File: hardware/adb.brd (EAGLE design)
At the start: 24.1 x 12.7 mm, 10 parts, among them U1 Tiny85-20-SMT

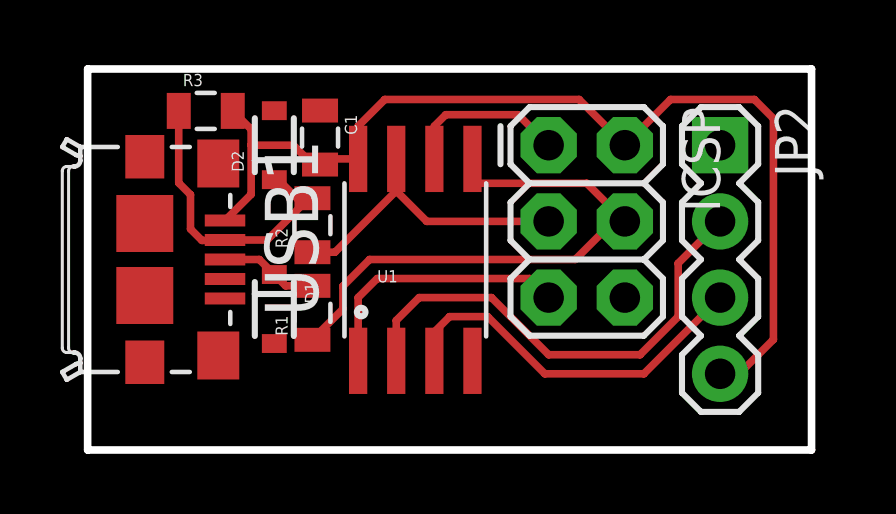
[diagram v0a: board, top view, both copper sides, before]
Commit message: hardware: bumped ICSP up, rearranged Rs and Ds.
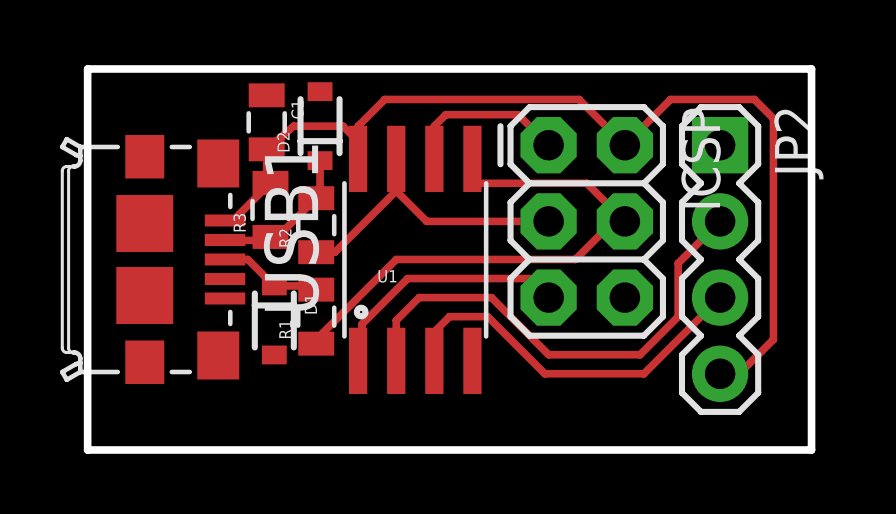
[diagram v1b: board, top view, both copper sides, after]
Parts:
- moved R3 3.95 mm to (6.10, 8.00), turned to 90 degrees
- moved C1 1.85 mm to (5.97, 10.9)
- moved D2 1.65 mm to (7.75, 10.8)
- moved D1 0.38 mm to (6.22, 4.32)
- moved R1 0.18 mm to (7.62, 4.45)
- moved R2 0.13 mm to (7.62, 7.49)
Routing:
- net D-: track 10.5 -> 4.93 mm
- net VCC: track 34.8 -> 33.4 mm
- net RESET: track 8.98 -> 8.39 mm
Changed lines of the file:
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@@
 </autorouter>
 <elements>
-<element name="C1" library="SparkFun-Capacitors" package="0805" value="1uF" x="7.747" y="10.414" rot="R270">
-<attribute name="PROD_ID" value="CAP-11625" x="7.747" y="10.414" size="1.778" layer="27" rot="R270" display="off"/>
+<element name="C1" library="SparkFun-Capacitors" package="0805" value="1uF" x="5.969" y="10.922" rot="R270">
+<attribute name="PROD_ID" value="CAP-11625" x="5.969" y="10.922" size="1.778" layer="27" rot="R270" display="off"/>
 </element>
-<element name="D1" library="SparkFun-DiscreteSemi" package="SOD-323" value="3.6V" x="6.223" y="4.699" rot="R270">
-<attribute name="PROD_ID" value="DIO-11284" x="6.223" y="4.699" size="1.778" layer="27" rot="R270" display="off"/>
+<element name="D1" library="SparkFun-DiscreteSemi" package="SOD-323" value="3.6V" x="6.223" y="4.318" rot="R270">
+<attribute name="PROD_ID" value="DIO-11284" x="6.223" y="4.318" size="1.778" layer="27" rot="R270" display="off"/>
 </element>
-<element name="D2" library="SparkFun-DiscreteSemi" package="SOD-323" value="3.6V" x="6.223" y="10.16" rot="R90">
-<attribute name="PROD_ID" value="DIO-11284" x="6.223" y="10.16" size="1.778" layer="27" rot="R90" display="off"/>
+<element name="D2" library="SparkFun-DiscreteSemi" package="SOD-323" value="3.6V" x="7.747" y="10.795" rot="R90">
+<attribute name="PROD_ID" value="DIO-11284" x="7.747" y="10.795" size="1.778" layer="27" rot="R90" display="off"/>
 </element>
 <element name="JP2" library="SparkFun-Connectors" package="1X04" value="" x="21.082" y="10.16" rot="R270"/>
-<element name="R1" library="SparkFun-Passives" package="0805" value="68R" x="7.493" y="4.572" rot="R90"/>
-<element name="R2" library="SparkFun-Passives" package="0805" value="68R" x="7.493" y="7.493" rot="R90"/>
+<element name="R1" library="SparkFun-Passives" package="0805" value="68R" x="7.62" y="4.445" rot="R90"/>
+<element name="R2" library="SparkFun-Passives" package="0805" value="68R" x="7.62" y="7.493" rot="R90"/>
 <element name="U1" library="SparkFun-DigitalIC" package="SO08-EIAJ" value="Tiny85-20-SMT" x="10.922" y="6.35">
 <attribute name="PROD_ID" value="IC-09092" x="10.922" y="6.35" size="1.778" layer="27" display="off"/>
@@
 <element name="ICSP" library="SparkFun-Connectors" package="2X3" value="" x="15.367" y="10.16" rot="R270"/>
 <element name="USB1" library="dangerousprototypes_devices" package="CONN_USB_MICRO-B" value="" x="1.905" y="6.35" rot="R270"/>
-<element name="R3" library="SparkFun-Passives" package="0805" value="2K2" x="3.937" y="11.303"/>
+<element name="R3" library="SparkFun-Passives" package="0805" value="2K2" x="6.096" y="8.001" rot="R90"/>
 </elements>
 <signals>
@@
 <contactref element="JP2" pad="4"/>
 <contactref element="USB1" pad="P1"/>
-<wire x1="4.58" y1="7.65" x2="5.45" y2="8.52" width="0.254" layer="1"/>
-<wire x1="5.45" y1="10.69" x2="5.45" y2="10.16" width="0.254" layer="1"/>
-<wire x1="5.45" y1="10.16" x2="5.45" y2="8.52" width="0.254" layer="1"/>
 <wire x1="17.907" y1="10.16" x2="16.383" y2="11.684" width="0.254" layer="1"/>
 <wire x1="22.86" y1="11.049" x2="22.86" y2="3.683" width="0.254" layer="1"/>
@@
 <wire x1="16.383" y1="11.684" x2="9.906" y2="11.684" width="0.254" layer="1"/>
 <wire x1="9.906" y1="11.684" x2="9.017" y2="10.795" width="0.254" layer="1"/>
-<wire x1="9.017" y1="10.795" x2="9.017" y2="9.7028" width="0.254" layer="1"/>
-<wire x1="7.747" y1="9.514" x2="7.504" y2="9.514" width="0.254" layer="1"/>
-<wire x1="7.504" y1="9.514" x2="6.858" y2="10.16" width="0.254" layer="1"/>
-<wire x1="6.858" y1="10.16" x2="5.45" y2="10.16" width="0.254" layer="1"/>
-<wire x1="7.747" y1="9.514" x2="7.9358" y2="9.7028" width="0.254" layer="1"/>
-<wire x1="7.9358" y1="9.7028" x2="9.017" y2="9.7028" width="0.254" layer="1"/>
+<wire x1="9.017" y1="10.795" x2="9.017" y2="10.287" width="0.254" layer="1"/>
 <contactref element="R3" pad="2"/>
+<wire x1="9.017" y1="10.287" x2="9.017" y2="9.7028" width="0.254" layer="1"/>
 <wire x1="17.907" y1="10.16" x2="19.431" y2="11.684" width="0.254" layer="1"/>
 <wire x1="19.431" y1="11.684" x2="22.225" y2="11.684" width="0.254" layer="1"/>
 <wire x1="22.225" y1="11.684" x2="22.86" y2="11.049" width="0.254" layer="1"/>
-<wire x1="5.45" y1="10.69" x2="4.837" y2="11.303" width="0.254" layer="1"/>
+<wire x1="5.969" y1="10.022" x2="6.869" y2="10.795" width="0.254" layer="1"/>
+<wire x1="6.869" y1="10.795" x2="8.509" y2="10.795" width="0.254" layer="1"/>
+<wire x1="8.509" y1="10.795" x2="9.017" y2="10.287" width="0.254" layer="1"/>
+<wire x1="4.58" y1="7.65" x2="4.845" y2="7.65" width="0.254" layer="1"/>
+<wire x1="4.845" y1="7.65" x2="6.096" y2="8.901" width="0.254" layer="1"/>
+<wire x1="5.969" y1="10.022" x2="5.969" y2="9.028" width="0.254" layer="1"/>
+<wire x1="5.969" y1="9.028" x2="6.096" y2="8.901" width="0.254" layer="1"/>
 </signal>
 <signal name="GND">
@@
 <wire x1="10.287" y1="9.7028" x2="10.287" y2="8.636" width="0.254" layer="1"/>
 <wire x1="10.287" y1="8.636" x2="8.244" y2="6.593" width="0.254" layer="1"/>
-<wire x1="7.493" y1="6.593" x2="8.244" y2="6.593" width="0.254" layer="1"/>
 <wire x1="10.287" y1="8.636" x2="11.303" y2="7.62" width="0.254" layer="1"/>
 <wire x1="11.303" y1="7.62" x2="15.367" y2="7.62" width="0.254" layer="1"/>
+<wire x1="7.62" y1="6.593" x2="8.244" y2="6.593" width="0.254" layer="1"/>
 </signal>
 <signal name="D-">
@@
 <contactref element="USB1" pad="P2"/>
 <wire x1="4.58" y1="7" x2="4.595" y2="6.985" width="0.254" layer="1"/>
-<wire x1="6.223" y1="9.01" x2="6.357" y2="9.01" width="0.254" layer="1"/>
-<wire x1="6.357" y1="9.01" x2="6.985" y2="8.382" width="0.254" layer="1"/>
-<wire x1="6.985" y1="8.382" x2="7.482" y2="8.382" width="0.254" layer="1"/>
-<wire x1="7.482" y1="8.382" x2="7.493" y2="8.393" width="0.254" layer="1"/>
-<wire x1="4.58" y1="7" x2="5.984" y2="7" width="0.254" layer="1"/>
-<wire x1="5.984" y1="7" x2="7.377" y2="8.393" width="0.254" layer="1"/>
-<wire x1="7.377" y1="8.393" x2="7.493" y2="8.393" width="0.254" layer="1"/>
 <contactref element="R3" pad="1"/>
-<wire x1="3.037" y1="11.303" x2="3.037" y2="8.901" width="0.254" layer="1"/>
-<wire x1="3.037" y1="8.901" x2="3.429" y2="8.509" width="0.254" layer="1"/>
-<wire x1="3.429" y1="8.509" x2="3.429" y2="7.366" width="0.254" layer="1"/>
-<wire x1="3.429" y1="7.366" x2="3.81" y2="6.985" width="0.254" layer="1"/>
-<wire x1="3.81" y1="6.985" x2="4.565" y2="6.985" width="0.254" layer="1"/>
-<wire x1="4.565" y1="6.985" x2="4.58" y2="7" width="0.254" layer="1"/>
+<wire x1="4.595" y1="6.985" x2="5.98" y2="6.985" width="0.254" layer="1"/>
+<wire x1="5.98" y1="6.985" x2="6.096" y2="7.101" width="0.254" layer="1"/>
+<wire x1="6.096" y1="7.101" x2="6.328" y2="7.101" width="0.254" layer="1"/>
+<wire x1="6.328" y1="7.101" x2="7.62" y2="8.393" width="0.254" layer="1"/>
+<wire x1="7.747" y1="9.645" x2="7.747" y2="8.52" width="0.254" layer="1"/>
+<wire x1="7.747" y1="8.52" x2="7.62" y2="8.393" width="0.254" layer="1"/>
 </signal>
 <signal name="D+">
@@
 <contactref element="D1" pad="C"/>
 <contactref element="USB1" pad="P3"/>
-<wire x1="4.58" y1="6.35" x2="5.722" y2="6.35" width="0.254" layer="1"/>
-<wire x1="5.722" y1="6.35" x2="6.223" y2="5.849" width="0.254" layer="1"/>
-<wire x1="6.223" y1="5.849" x2="6.6" y2="5.472" width="0.254" layer="1"/>
-<wire x1="6.6" y1="5.472" x2="7.493" y2="5.472" width="0.254" layer="1"/>
+<wire x1="4.58" y1="6.35" x2="5.341" y2="6.35" width="0.254" layer="1"/>
+<wire x1="5.341" y1="6.35" x2="6.223" y2="5.468" width="0.254" layer="1"/>
+<wire x1="6.223" y1="5.468" x2="7.497" y2="5.468" width="0.254" layer="1"/>
+<wire x1="7.497" y1="5.468" x2="7.62" y2="5.345" width="0.254" layer="1"/>
 </signal>
 <signal name="MOSI">
@@
 <wire x1="17.907" y1="7.62" x2="17.526" y2="7.62" width="0.254" layer="1"/>
 <wire x1="17.526" y1="7.62" x2="16.256" y2="6.35" width="0.254" layer="1"/>
-<wire x1="7.493" y1="3.672" x2="7.493" y2="3.683" width="0.254" layer="1"/>
-<wire x1="7.493" y1="3.683" x2="8.509" y2="4.699" width="0.254" layer="1"/>
-<wire x1="8.509" y1="4.699" x2="8.509" y2="5.461" width="0.254" layer="1"/>
-<wire x1="8.509" y1="5.461" x2="9.398" y2="6.35" width="0.254" layer="1"/>
-<wire x1="9.398" y1="6.35" x2="16.256" y2="6.35" width="0.254" layer="1"/>
+<wire x1="10.287" y1="6.35" x2="16.256" y2="6.35" width="0.254" layer="1"/>
+<wire x1="10.287" y1="6.35" x2="7.62" y2="3.683" width="0.254" layer="1"/>
+<wire x1="7.62" y1="3.683" x2="7.62" y2="3.545" width="0.254" layer="1"/>
 </signal>
 <signal name="MISO">
@@
 <contactref element="U1" pad="1"/>
 <contactref element="ICSP" pad="5"/>
-<wire x1="9.017" y1="2.9718" x2="9.017" y2="5.08" width="0.254" layer="1"/>
-<wire x1="9.017" y1="5.08" x2="9.652" y2="5.715" width="0.254" layer="1"/>
-<wire x1="9.652" y1="5.715" x2="14.732" y2="5.715" width="0.254" layer="1"/>
+<wire x1="10.668" y1="5.715" x2="14.732" y2="5.715" width="0.254" layer="1"/>
 <wire x1="14.732" y1="5.715" x2="15.367" y2="5.08" width="0.254" layer="1"/>
+<wire x1="10.668" y1="5.715" x2="9.144" y2="4.191" width="0.254" layer="1"/>
+<wire x1="9.144" y1="4.191" x2="9.144" y2="3.937" width="0.254" layer="1"/>
+<wire x1="9.144" y1="3.937" x2="9.017" y2="3.81" width="0.254" layer="1"/>
+<wire x1="9.017" y1="3.81" x2="9.017" y2="2.9718" width="0.254" layer="1"/>
 </signal>
 <signal name="N$2">

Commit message: hardware: AVR reset pulled high.
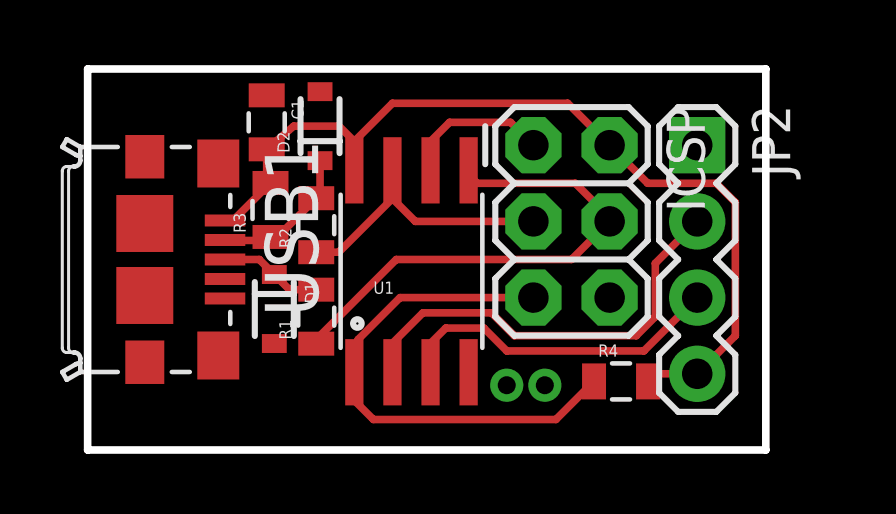
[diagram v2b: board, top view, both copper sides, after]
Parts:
- added R4: 10K, SparkFun-Passives:0805
- moved JP2 0.76 mm to (20.3, 10.2)
- moved ICSP 0.51 mm to (14.9, 10.2)
- moved U1 0.40 mm to (10.8, 5.97)
- moved D1 0.38 mm to (6.22, 4.70)
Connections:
- net RESET: now also R4.1
- net VCC: now also R4.2
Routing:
- net RESET: track 8.39 -> 17.3 mm
- net VCC: track 33.4 -> 30.4 mm
- net N$5: track 16.1 -> 14.5 mm
- net MOSI: track 18.6 -> 17.1 mm
- net N$2: track 12.5 -> 11.1 mm
- net SCK: track 10.1 -> 9.24 mm
- net MISO: track 5.48 -> 4.97 mm
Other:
- board size 24.1 x 12.7 mm -> 22.6 x 12.7 mm

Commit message: hardware: tweaks; Eagle 7.2 upgrade.
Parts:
- moved D2 0.38 mm to (7.75, 10.4)
- moved R2 0.18 mm to (7.75, 7.37)
- moved R3 0.18 mm to (6.22, 7.87)
- moved C1 0.13 mm to (5.97, 10.8)

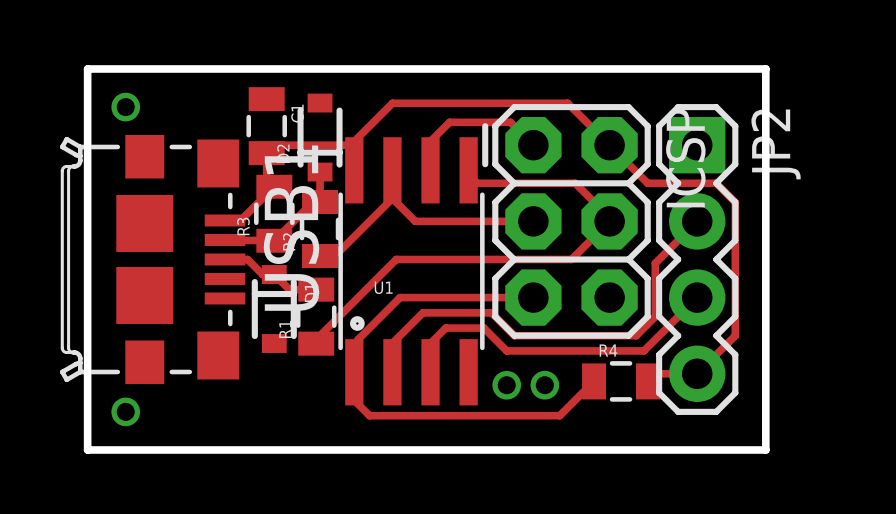
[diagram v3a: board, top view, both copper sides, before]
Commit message: hardware: polish; silk screen text etc.
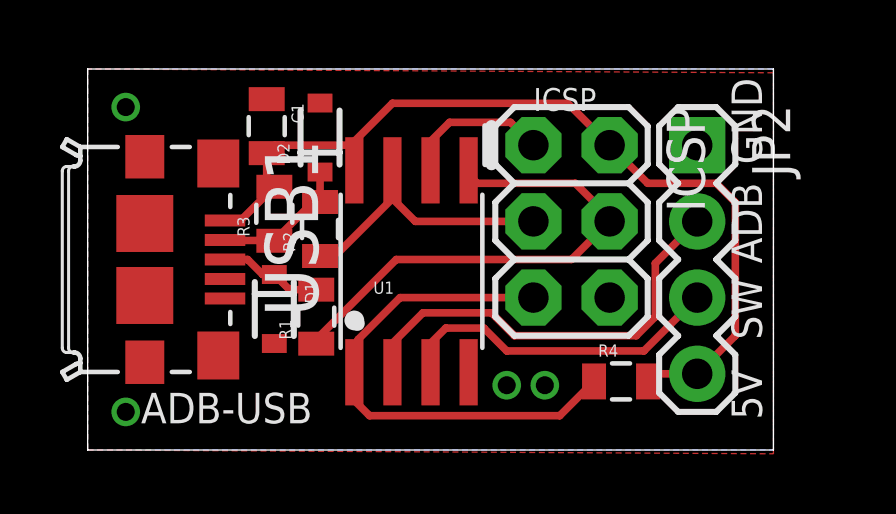
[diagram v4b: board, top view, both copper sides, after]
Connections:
- net N$2 renamed PB4
- net N$5 renamed PB3
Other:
- board size 22.6 x 12.7 mm -> 22.9 x 12.7 mm
- board text added: "5V"
- board text added: "ADB"
- board text added: "ADB-USB"
- board text added: "Apple Extended Keyboard II USB adapter @pda 2015"
- board text added: "GND"
- board text added: "ICSP"
- board text added: "SW"
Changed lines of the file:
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@@
 <layer number="20" name="Dimension" color="15" fill="1" visible="yes" active="yes"/>
 <layer number="21" name="tPlace" color="7" fill="1" visible="no" active="yes"/>
-<layer number="22" name="bPlace" color="7" fill="1" visible="yes" active="yes"/>
+<layer number="22" name="bPlace" color="7" fill="1" visible="no" active="yes"/>
 <layer number="23" name="tOrigins" color="15" fill="1" visible="yes" active="yes"/>
 <layer number="24" name="bOrigins" color="15" fill="1" visible="yes" active="yes"/>
@@
 <layer number="29" name="tStop" color="7" fill="3" visible="yes" active="yes"/>
 <layer number="30" name="bStop" color="7" fill="6" visible="yes" active="yes"/>
-<layer number="31" name="tCream" color="7" fill="4" visible="no" active="yes"/>
-<layer number="32" name="bCream" color="7" fill="5" visible="no" active="yes"/>
-<layer number="33" name="tFinish" color="6" fill="3" visible="no" active="yes"/>
-<layer number="34" name="bFinish" color="6" fill="6" visible="no" active="yes"/>
-<layer number="35" name="tGlue" color="7" fill="4" visible="no" active="yes"/>
-<layer number="36" name="bGlue" color="7" fill="5" visible="no" active="yes"/>
-<layer number="37" name="tTest" color="7" fill="1" visible="no" active="yes"/>
-<layer number="38" name="bTest" color="7" fill="1" visible="no" active="yes"/>
+<layer number="31" name="tCream" color="7" fill="4" visible="yes" active="yes"/>
+<layer number="32" name="bCream" color="7" fill="5" visible="yes" active="yes"/>
+<layer number="33" name="tFinish" color="6" fill="3" visible="yes" active="yes"/>
+<layer number="34" name="bFinish" color="6" fill="6" visible="yes" active="yes"/>
+<layer number="35" name="tGlue" color="7" fill="4" visible="yes" active="yes"/>
+<layer number="36" name="bGlue" color="7" fill="5" visible="yes" active="yes"/>
+<layer number="37" name="tTest" color="7" fill="1" visible="yes" active="yes"/>
+<layer number="38" name="bTest" color="7" fill="1" visible="yes" active="yes"/>
 <layer number="39" name="tKeepout" color="4" fill="11" visible="yes" active="yes"/>
 <layer number="40" name="bKeepout" color="1" fill="11" visible="yes" active="yes"/>
@@
 <layer number="42" name="bRestrict" color="1" fill="10" visible="yes" active="yes"/>
 <layer number="43" name="vRestrict" color="2" fill="10" visible="yes" active="yes"/>
-<layer number="44" name="Drills" color="7" fill="1" visible="yes" active="yes"/>
+<layer number="44" name="Drills" color="7" fill="1" visible="no" active="yes"/>
 <layer number="45" name="Holes" color="7" fill="1" visible="yes" active="yes"/>
 <layer number="46" name="Milling" color="3" fill="1" visible="yes" active="yes"/>
-<layer number="47" name="Measures" color="7" fill="1" visible="no" active="yes"/>
-<layer number="48" name="Document" color="7" fill="1" visible="no" active="yes"/>
-<layer number="49" name="Reference" color="7" fill="1" visible="no" active="yes"/>
+<layer number="47" name="Measures" color="7" fill="1" visible="yes" active="yes"/>
+<layer number="48" name="Document" color="7" fill="1" visible="yes" active="yes"/>
+<layer number="49" name="Reference" color="7" fill="1" visible="yes" active="yes"/>
 <layer number="50" name="dxf" color="7" fill="1" visible="no" active="no"/>
-<layer number="51" name="tDocu" color="7" fill="1" visible="no" active="yes"/>
-<layer number="52" name="bDocu" color="7" fill="1" visible="no" active="yes"/>
+<layer number="51" name="tDocu" color="7" fill="1" visible="yes" active="yes"/>
+<layer number="52" name="bDocu" color="7" fill="1" visible="yes" active="yes"/>
 <layer number="53" name="tGND_GNDA" color="7" fill="9" visible="no" active="no"/>
 <layer number="54" name="bGND_GNDA" color="1" fill="9" visible="no" active="no"/>
@@
 <board>
 <plain>
-<wire x1="0" y1="12.7" x2="22.606" y2="12.7" width="0.254" layer="20"/>
-<wire x1="22.606" y1="12.7" x2="22.606" y2="0" width="0.254" layer="20"/>
-<wire x1="22.606" y1="0" x2="0" y2="0" width="0.254" layer="20"/>
-<wire x1="0" y1="0" x2="0" y2="12.7" width="0.254" layer="20"/>
+<wire x1="0" y1="12.7" x2="22.86" y2="12.7" width="0" layer="20"/>
+<wire x1="22.86" y1="12.7" x2="22.86" y2="0" width="0" layer="20"/>
+<wire x1="22.86" y1="0" x2="0" y2="0" width="0" layer="20"/>
+<wire x1="0" y1="0" x2="0" y2="12.7" width="0" layer="20"/>
+<text x="1.778" y="0.889" size="1.016" layer="121" font="vector" ratio="10">ADB-USB</text>
+<text x="22.479" y="1.016" size="1.016" layer="121" ratio="10" rot="R90">5V</text>
+<text x="22.479" y="9.525" size="1.016" layer="121" ratio="10" rot="R90">GND</text>
+<text x="22.479" y="6.223" size="1.016" layer="121" ratio="10" rot="R90">ADB</text>
+<text x="22.479" y="3.683" size="1.016" layer="121" ratio="10" rot="R90">SW</text>
+<text x="14.859" y="11.303" size="0.762" layer="121" ratio="10">ICSP</text>
+<wire x1="13.462" y1="10.795" x2="13.462" y2="9.525" width="0.4064" layer="121"/>
+<text x="7.62" y="3.81" size="1.016" layer="122" font="vector" ratio="10" rot="MR0" align="bottom-center">Apple Extended
+Keyboard II
+USB adapter
+@pda 2015</text>
+<circle x="8.89" y="4.318" radius="0.127" width="0.4064" layer="121"/>
 </plain>
 <attributes>
@@
 <vertex x="0" y="12.7"/>
 <vertex x="0" y="0"/>
-<vertex x="22.606" y="0"/>
-<vertex x="22.606" y="12.7"/>
+<vertex x="22.86" y="-0.127"/>
+<vertex x="22.86" y="12.573"/>
 </polygon>
 <polygon width="0.254" layer="16">
 <vertex x="0" y="12.7"/>
 <vertex x="0" y="0"/>
-<vertex x="22.606" y="0"/>
-<vertex x="22.606" y="12.7"/>
+<vertex x="22.86" y="0"/>
+<vertex x="22.86" y="12.7"/>
 </polygon>
 <via x="13.97" y="2.159" extent="1-16" drill="0.6"/>
@@
 <wire x1="15.737" y1="1.143" x2="16.88" y2="2.286" width="0.254" layer="1"/>
 </signal>
-<signal name="N$2">
+<signal name="PB4">
 <contactref element="U1" pad="3"/>
 <contactref element="JP2" pad="3"/>
@@
 <wire x1="13.208" y1="4.064" x2="13.97" y2="3.302" width="0.254" layer="1"/>
 </signal>
-<signal name="N$5">
+<signal name="PB3">
 <contactref element="U1" pad="2"/>
 <contactref element="JP2" pad="2"/>
@@
 </board>
 </drawing>
+<compatibility>
+<note version="6.3" minversion="6.2.2" severity="warning">
+Since Version 6.2.2 text objects can contain more than one line,
+which will not be processed correctly with this version.
+</note>
+</compatibility>
 </eagle>
